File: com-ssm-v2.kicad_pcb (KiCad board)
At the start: 4 copper layers, 98 x 84 mm, 23 parts, among them J1 RST_JMP, J2 DEBUG CONN, J3 PROGRAMMING PORT, P1 CONN_02X10, P2 CONN_02X10, SW1 SW_RST, U1 SN65HVD230, U2 ATMEGA32M1-MU, Y1 8MHz

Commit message: Pour power planes
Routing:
- added copper zone on VCC, net +3V3
- added copper zone on GND, net GND
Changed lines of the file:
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@@
   (general
     (links 88)
-    (no_connects 27)
+    (no_connects 5)
     (area 99.924999 46.723 221.946906 146.795)
     (thickness 1.6)
@@
   (segment (start 139 62.75) (end 139.5 62.25) (width 0.25) (layer B.Cu) (net 88))
   (segment (start 134.25 62.75) (end 139 62.75) (width 0.25) (layer B.Cu) (net 88))
-  (segment (start 126.492 61.492) (end 127.75 62.75) (width 0.25) (layer B.Cu) (net 88) (status 400000))
+  (segment (start 126.492 61.492) (end 127.75 62.75) (width 0.25) (layer B.Cu) (net 88))
   (segment (start 127.75 62.75) (end 134 62.75) (width 0.25) (layer B.Cu) (net 88))
   (segment (start 134 62.75) (end 134.25 62.75) (width 0.25) (layer B.Cu) (net 88))
@@
   (segment (start 139.5 62.25) (end 141.25 62.25) (width 0.25) (layer F.Cu) (net 88))
   (via (at 139.5 62.25) (size 0.7) (drill 0.4) (layers F.Cu B.Cu) (net 88))
-  (segment (start 126.492 60.833) (end 126.492 61.492) (width 0.25) (layer B.Cu) (net 88) (status C00000))
+  (segment (start 126.492 60.833) (end 126.492 61.492) (width 0.25) (layer B.Cu) (net 88))
   (segment (start 145 103.89) (end 148.5 103.89) (width 0.25) (layer F.Cu) (net 88))
   (segment (start 148.5 103.89) (end 153.71 103.89) (width 0.25) (layer F.Cu) (net 88))
@@
   (segment (start 142 56) (end 143 57) (width 0.25) (layer F.Cu) (net 91))
   (segment (start 143 57) (end 143 61) (width 0.25) (layer F.Cu) (net 91))
-  (segment (start 129.032 58.293) (end 129.032 56.968) (width 0.25) (layer F.Cu) (net 91) (status 400000))
+  (segment (start 129.032 58.293) (end 129.032 56.968) (width 0.25) (layer F.Cu) (net 91))
   (segment (start 151.125 104.875) (end 151.25 105) (width 0.25) (layer B.Cu) (net 91))
   (segment (start 151.125 104.625) (end 151.125 104.875) (width 0.25) (layer B.Cu) (net 91))
@@
   (segment (start 141.4 108) (end 141.8 108.4) (width 0.25) (layer F.Cu) (net 91))
   (segment (start 172.017 93.288) (end 170.967 93.288) (width 0.25) (layer F.Cu) (net 94))
+  (zone (net 1) (net_name GND) (layer GND) (hatch edge 0.508)
+    (connect_pads (clearance 0.508))
+    (min_thickness 0.254)
+    (fill yes (arc_segments 16) (thermal_gap 0.508) (thermal_bridge_width 0.508))
+    (polygon
+      (pts
+        (xy 200 48.75) (xy 199.5 136) (xy 98 136.25) (xy 98.249993 48.252445)
+      )
+    )
+  )
+  (zone (net 1) (net_name GND) (layer GND) (hatch edge 0.508)
+    (connect_pads (clearance 0.508))
+    (min_thickness 0.254)
+    (fill yes (arc_segments 16) (thermal_gap 0.508) (thermal_bridge_width 0.508))
+    (polygon
+      (pts
+        (xy 97.75 48.25) (xy 98.25 48.25) (xy 98.249993 48.252445)
+      )
+    )
+  )
+  (zone (net 2) (net_name +3V3) (layer VCC) (hatch edge 0.508)
+    (connect_pads (clearance 0.508))
+    (min_thickness 0.254)
+    (fill yes (arc_segments 16) (thermal_gap 0.508) (thermal_bridge_width 0.508))
+    (polygon
+      (pts
+        (xy 200.260922 47.985718) (xy 201.25 137.25) (xy 95.5 138) (xy 97.5 46)
+      )
+    )
+  )
+  (zone (net 2) (net_name +3V3) (layer VCC) (hatch edge 0.508)
+    (connect_pads (clearance 0.508))
+    (min_thickness 0.254)
+    (fill yes (arc_segments 16) (thermal_gap 0.508) (thermal_bridge_width 0.508))
+    (polygon
+      (pts
+        (xy 201 48) (xy 200.260922 47.985718) (xy 200.25 47)
+      )
+    )
+  )
 )

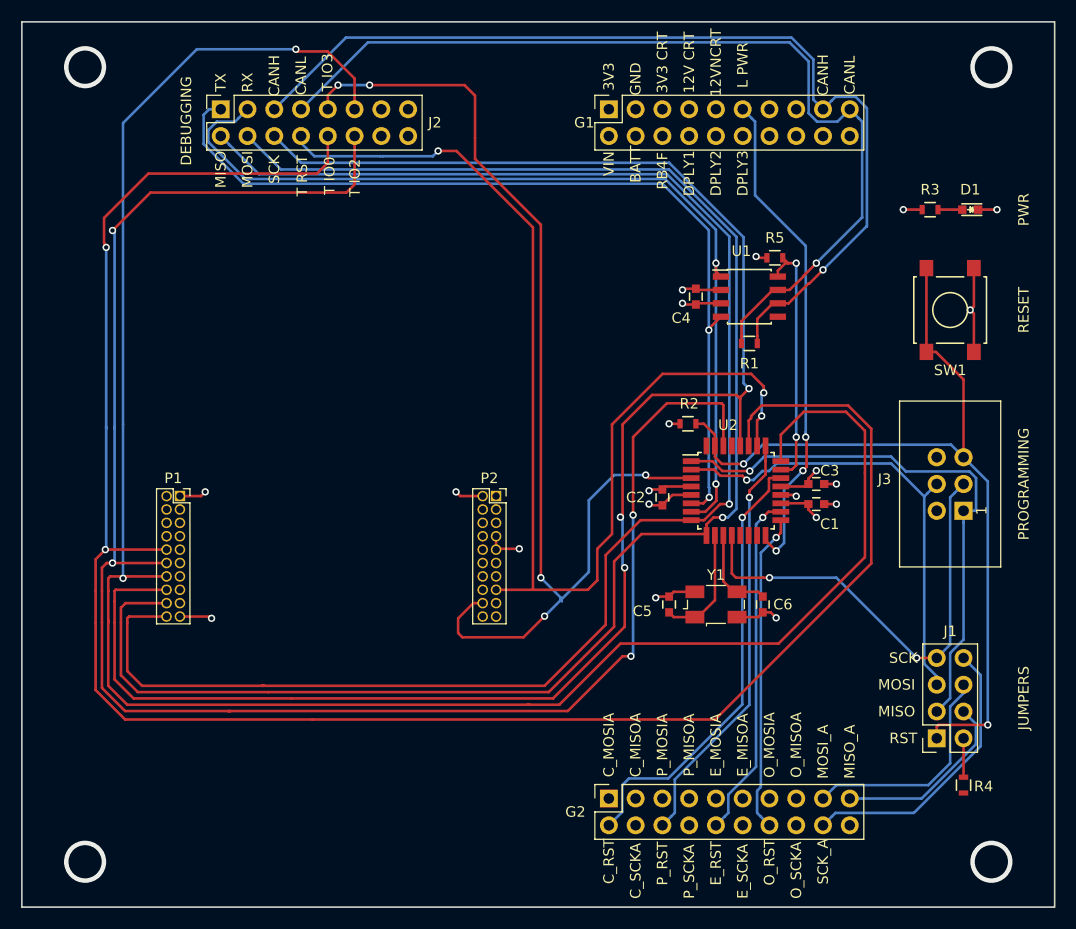
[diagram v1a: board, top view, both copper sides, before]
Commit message: Fixed missing connections; DRC check passes
Please review
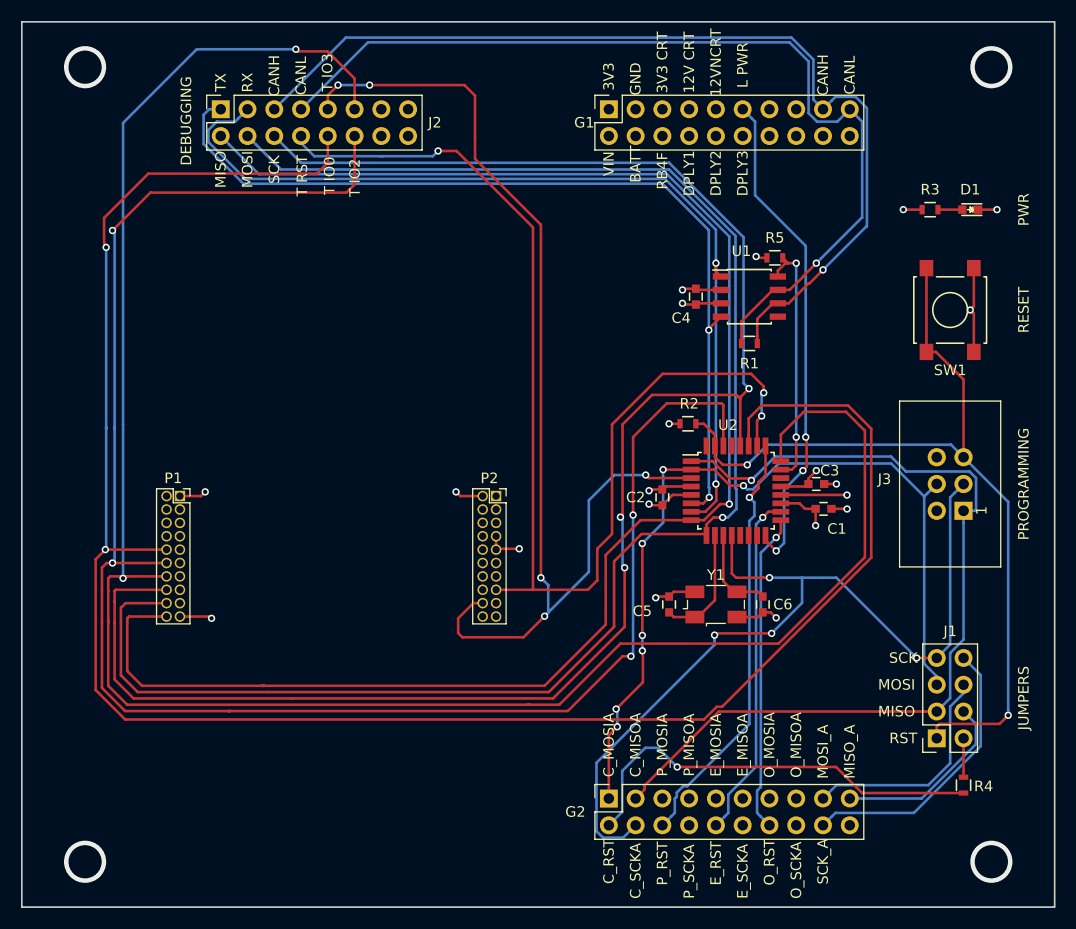
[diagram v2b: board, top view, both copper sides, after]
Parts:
- moved C1 0.82 mm to (176.1, 96.2)
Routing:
- net /SCK_A: track 43.9 -> 83.6 mm, vias 2 -> 4
- net /MOSI_A: track 44.5 -> 81.4 mm, vias 1 -> 7
- net /MISO_A: track 53.2 -> 86.1 mm
- net GND: track 39.8 -> 44.9 mm
- net /RST: track 81.7 -> 84.0 mm
- net Net-(U2-Pad22): track 1.05 -> 0.00 mm
- net /TRC_GPIO3: track 104.6 -> 105.6 mm
- net +3V3: track 22.8 -> 23.7 mm
- net /COM_RST: track 41.5 -> 40.8 mm
- net /PAY_RST: track 40.1 -> 40.7 mm
